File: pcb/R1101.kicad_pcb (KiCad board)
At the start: 2 copper layers, 33 x 51 mm, 4 parts, among them J1 COMPUTE_MOD_1, U1 PHOTON_SMD

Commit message: added silkscreen art
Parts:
- added A1: ART, pluggee:pluggeeLabsIcon-16X8, B.Cu at (150.2, 116.0)
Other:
- board text added: "R1101 v1.0 particle.io Photon Interposer plugg.ee Labs LLC 2017 http://plugg.ee"
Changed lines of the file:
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@@
     (area 125.924999 78.924999 159.075001 130.075001)
     (thickness 1.6)
-    (drawings 11)
+    (drawings 12)
     (tracks 62)
     (zones 0)
-    (modules 4)
+    (modules 5)
     (nets 14)
   )
   (page A4)
   (layers
-    (0 F.Cu signal)
-    (31 B.Cu signal)
+    (0 F.Cu signal hide)
+    (31 B.Cu signal hide)
     (32 B.Adhes user)
     (33 F.Adhes user)
@@
       (net 13 /pUSB-))
   )
+  (module pluggee:pluggeeLabsIcon-16X8 (layer B.Cu)
+    (at 150.2 116 90)
+    (fp_text reference A1 (at 0 0 90) (layer B.SilkS) hide
+      (effects (font (thickness 0.3)) (justify mirror))
+    )
+    (fp_text value ART (at 0.75 0 90) (layer B.SilkS) hide
+      (effects (font (thickness 0.3)) (justify mirror))
+    )
+    (fp_poly (pts (xy 7.9375 2.672447) (xy 7.391846 2.000251) (xy 5.524684 2.00025) (xy 3.657522 2.00025)
+      (xy 3.593078 2.109474) (xy 3.52497 2.195927) (xy 3.432187 2.280637) (xy 3.399991 2.30383)
+      (xy 3.316515 2.352706) (xy 3.240573 2.375634) (xy 3.144042 2.378874) (xy 3.079872 2.375112)
+      (xy 2.891651 2.333311) (xy 2.736834 2.241349) (xy 2.622568 2.10544) (xy 2.556003 1.931796)
+      (xy 2.553114 1.917327) (xy 2.546188 1.737138) (xy 2.590288 1.579105) (xy 2.675815 1.4471)
+      (xy 2.793167 1.344997) (xy 2.932745 1.276667) (xy 3.084946 1.245984) (xy 3.240171 1.25682)
+      (xy 3.38882 1.313047) (xy 3.521291 1.418539) (xy 3.585131 1.501041) (xy 3.661888 1.619251)
+      (xy 5.388818 1.619251) (xy 5.776474 1.618983) (xy 6.104767 1.618114) (xy 6.377835 1.61655)
+      (xy 6.599813 1.614192) (xy 6.774837 1.610945) (xy 6.907042 1.606712) (xy 7.000566 1.601397)
+      (xy 7.059543 1.594903) (xy 7.08811 1.587134) (xy 7.091638 1.579563) (xy 7.065771 1.544591)
+      (xy 7.005869 1.467368) (xy 6.917656 1.355153) (xy 6.806857 1.215207) (xy 6.679194 1.054789)
+      (xy 6.57845 0.928688) (xy 6.089372 0.317501) (xy 4.052748 0.317701) (xy 2.016125 0.317902)
+      (xy 1.962419 0.412289) (xy 1.861679 0.529425) (xy 1.722559 0.611213) (xy 1.562839 0.65194)
+      (xy 1.400298 0.645894) (xy 1.315286 0.620207) (xy 1.142547 0.516676) (xy 1.016597 0.370744)
+      (xy 0.964805 0.264947) (xy 0.929341 0.094751) (xy 0.947704 -0.069007) (xy 1.01162 -0.217747)
+      (xy 1.112814 -0.34289) (xy 1.243011 -0.435856) (xy 1.393938 -0.488067) (xy 1.557318 -0.490942)
+      (xy 1.666226 -0.46231) (xy 1.752506 -0.416273) (xy 1.847441 -0.346197) (xy 1.935782 -0.266066)
+      (xy 2.00228 -0.189862) (xy 2.031684 -0.131569) (xy 2.032 -0.126908) (xy 2.063614 -0.119836)
+      (xy 2.157925 -0.113631) (xy 2.314135 -0.108305) (xy 2.531448 -0.103871) (xy 2.809065 -0.10034)
+      (xy 3.14619 -0.097725) (xy 3.542025 -0.096037) (xy 3.995772 -0.095289) (xy 4.137175 -0.09525)
+      (xy 6.242351 -0.095249) (xy 7.089925 1.003648) (xy 7.9375 2.102545) (xy 7.9375 -0.977376)
+      (xy 7.580312 -1.408741) (xy 7.223125 -1.840105) (xy 5.090399 -1.840802) (xy 2.957674 -1.8415)
+      (xy 2.922728 -1.735612) (xy 2.845738 -1.592506) (xy 2.729856 -1.488125) (xy 2.587116 -1.423263)
+      (xy 2.429552 -1.398715) (xy 2.269197 -1.415274) (xy 2.118086 -1.473735) (xy 1.988253 -1.574891)
+      (xy 1.91778 -1.669291) (xy 1.850254 -1.839804) (xy 1.839916 -2.010188) (xy 1.881276 -2.170131)
+      (xy 1.968845 -2.309316) (xy 2.097132 -2.417429) (xy 2.260649 -2.484157) (xy 2.359484 -2.499199)
+      (xy 2.540921 -2.482357) (xy 2.701006 -2.407286) (xy 2.832592 -2.277645) (xy 2.854881 -2.245459)
+      (xy 2.931638 -2.12725) (xy 5.162894 -2.12725) (xy 5.59363 -2.127189) (xy 5.965311 -2.126931)
+      (xy 6.282381 -2.126361) (xy 6.549286 -2.125366) (xy 6.770468 -2.123831) (xy 6.950374 -2.121642)
+      (xy 7.093448 -2.118685) (xy 7.204134 -2.114845) (xy 7.286877 -2.110009) (xy 7.346122 -2.104062)
+      (xy 7.386313 -2.096891) (xy 7.411895 -2.08838) (xy 7.427313 -2.078416) (xy 7.435637 -2.068873)
+      (xy 7.47392 -2.021825) (xy 7.544397 -1.941065) (xy 7.635882 -1.839258) (xy 7.707312 -1.761298)
+      (xy 7.9375 -1.512098) (xy 7.9375 -4.15925) (xy -7.9375 -4.15925) (xy -7.9375 -2.688196)
+      (xy -7.509706 -2.12725) (xy -5.63124 -2.12725) (xy -3.752773 -2.127249) (xy -3.688329 -2.236473)
+      (xy -3.571643 -2.37785) (xy -3.423244 -2.472213) (xy -3.255893 -2.515964) (xy -3.082352 -2.505506)
+      (xy -2.935025 -2.448817) (xy -2.78592 -2.335518) (xy -2.692871 -2.193123) (xy -2.653784 -2.018042)
+      (xy -2.652212 -1.964385) (xy -2.658491 -1.84716) (xy -2.681995 -1.763529) (xy -2.73228 -1.684047)
+      (xy -2.750828 -1.660542) (xy -2.881344 -1.528115) (xy -3.019707 -1.451293) (xy -3.180728 -1.422562)
+      (xy -3.221213 -1.421954) (xy -3.40284 -1.448299) (xy -3.555673 -1.51942) (xy -3.669787 -1.628645)
+      (xy -3.734757 -1.767283) (xy -3.753384 -1.8415) (xy -5.480317 -1.8415) (xy -5.804828 -1.84115)
+      (xy -6.109463 -1.840144) (xy -6.38846 -1.838547) (xy -6.636056 -1.836426) (xy -6.846485 -1.833845)
+      (xy -7.013986 -1.830869) (xy -7.132794 -1.827565) (xy -7.197146 -1.823999) (xy -7.207251 -1.821876)
+      (xy -7.189178 -1.792127) (xy -7.138199 -1.718128) (xy -7.059177 -1.606677) (xy -6.956972 -1.464575)
+      (xy -6.836444 -1.298619) (xy -6.702454 -1.115609) (xy -6.696495 -1.107501) (xy -6.185739 -0.41275)
+      (xy -2.125889 -0.41275) (xy -2.090247 -0.490975) (xy -2.027738 -0.573654) (xy -1.924235 -0.657612)
+      (xy -1.800249 -0.728336) (xy -1.703337 -0.76475) (xy -1.545731 -0.777984) (xy -1.393042 -0.737467)
+      (xy -1.255042 -0.652763) (xy -1.141503 -0.533435) (xy -1.062197 -0.389048) (xy -1.026896 -0.229165)
+      (xy -1.034201 -0.109895) (xy -1.094207 0.056773) (xy -1.199417 0.19582) (xy -1.337729 0.299435)
+      (xy -1.497039 0.359809) (xy -1.665245 0.36913) (xy -1.74984 0.351926) (xy -1.85936 0.303082)
+      (xy -1.968986 0.228669) (xy -2.059232 0.144309) (xy -2.110612 0.065628) (xy -2.111996 0.061545)
+      (xy -2.117415 0.049345) (xy -2.12838 0.038873) (xy -2.149438 0.029997) (xy -2.185134 0.022586)
+      (xy -2.240013 0.016507) (xy -2.318623 0.01163) (xy -2.425507 0.00782) (xy -2.565212 0.004948)
+      (xy -2.742284 0.002881) (xy -2.961268 0.001487) (xy -3.226711 0.000633) (xy -3.543157 0.000189)
+      (xy -3.915152 0.000023) (xy -4.232906 0) (xy -6.334282 0) (xy -7.096204 -1.005741)
+      (xy -7.264754 -1.228202) (xy -7.422305 -1.436092) (xy -7.564506 -1.623676) (xy -7.687006 -1.785216)
+      (xy -7.785453 -1.914975) (xy -7.855499 -2.007217) (xy -7.892791 -2.056203) (xy -7.896803 -2.061429)
+      (xy -7.907366 -2.063054) (xy -7.91597 -2.034729) (xy -7.922793 -1.971604) (xy -7.928017 -1.868832)
+      (xy -7.931821 -1.72156) (xy -7.934385 -1.524941) (xy -7.935889 -1.274125) (xy -7.936491 -0.992187)
+      (xy -7.9375 0.127) (xy -7.33864 0.127) (xy -6.661758 0.919663) (xy -5.984875 1.712326)
+      (xy -3.836949 1.713413) (xy -1.689023 1.714501) (xy -1.624579 1.605277) (xy -1.511671 1.469556)
+      (xy -1.363986 1.373267) (xy -1.198946 1.326564) (xy -1.141587 1.323789) (xy -0.969591 1.351361)
+      (xy -0.819933 1.431996) (xy -0.689389 1.562438) (xy -0.604399 1.712563) (xy -0.574047 1.873662)
+      (xy -0.593346 2.034858) (xy -0.657311 2.185273) (xy -0.760959 2.314027) (xy -0.899304 2.410244)
+      (xy -1.067361 2.463044) (xy -1.104094 2.467437) (xy -1.265806 2.454635) (xy -1.421591 2.395068)
+      (xy -1.550438 2.298656) (xy -1.603375 2.231661) (xy -1.666875 2.129697) (xy -3.893755 2.128474)
+      (xy -6.120634 2.12725) (xy -6.811924 1.317625) (xy -7.503215 0.508) (xy -7.9375 0.508)
+      (xy -7.9375 4.15925) (xy 7.9375 4.15925) (xy 7.9375 2.672447)) (layer B.SilkS) (width 0.01))
+  )
+  (gr_text "R1101 v1.0\nparticle.io Photon Interposer\nplugg.ee Labs LLC 2017\nhttp://plugg.ee" (at 141.2 124.2 270) (layer B.SilkS)
+    (effects (font (size 1.2 1.2) (thickness 0.2)) (justify left mirror))
+  )
   (gr_arc (start 128 128) (end 128 130) (angle 90) (layer Edge.Cuts) (width 0.15))

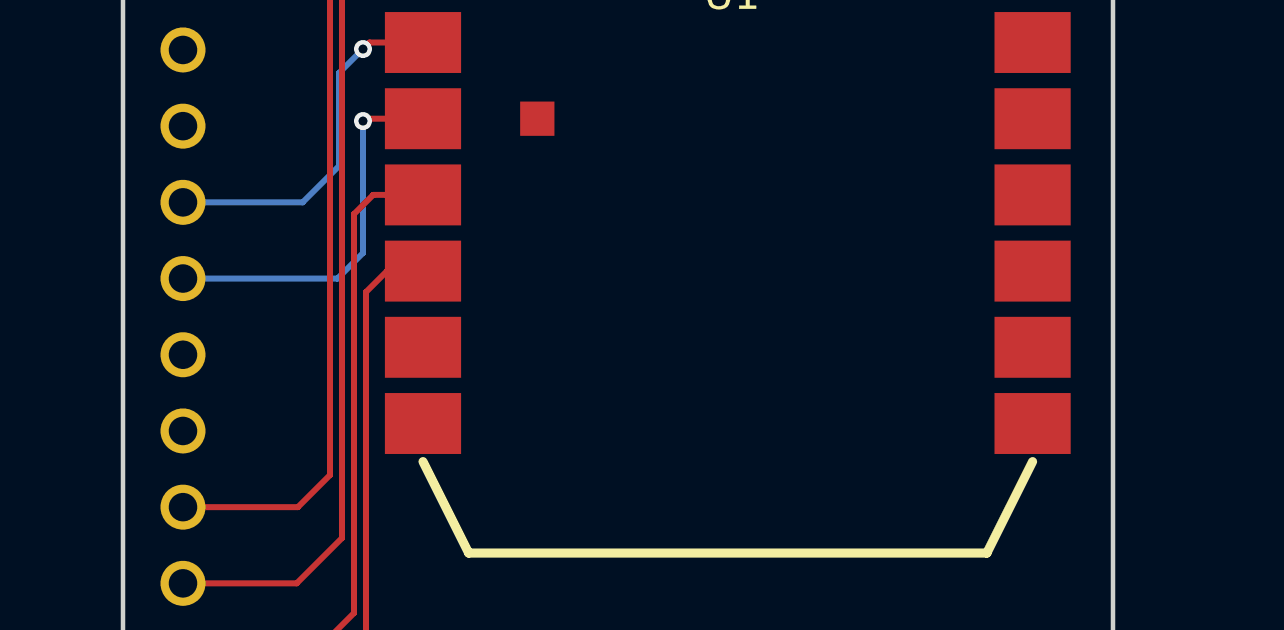
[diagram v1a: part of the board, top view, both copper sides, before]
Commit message: connected I2C
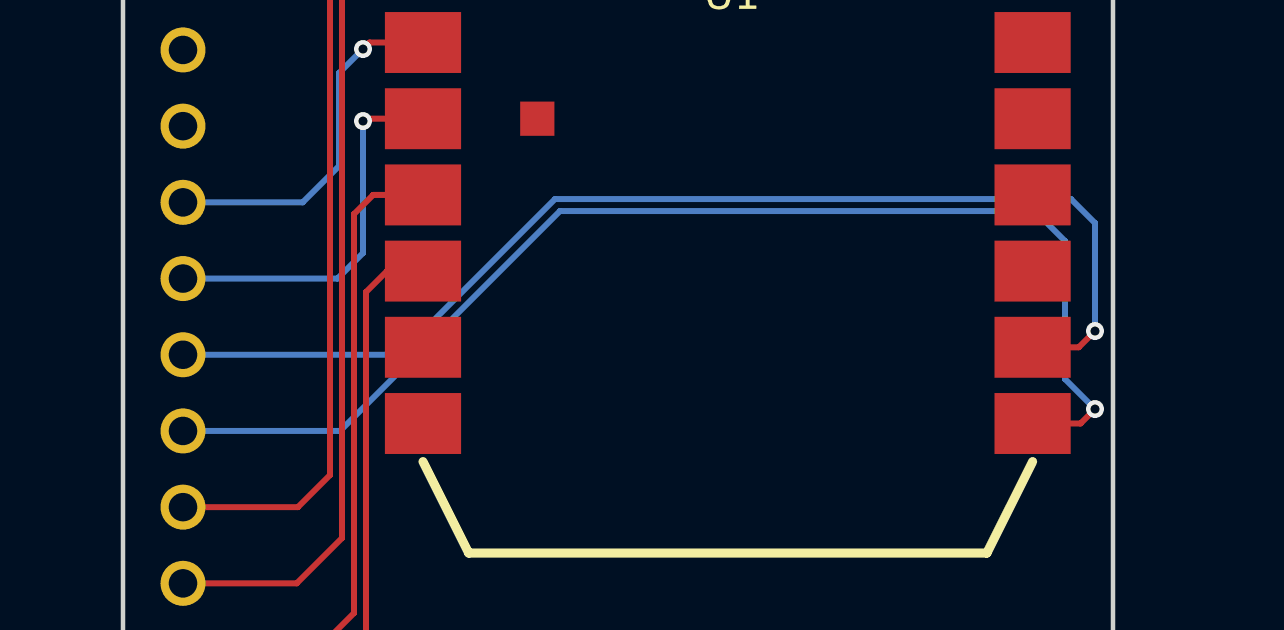
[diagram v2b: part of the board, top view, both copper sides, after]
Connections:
- J1 pad 11: (no net) -> /SCK
- J1 pad 12: (no net) -> /SDA
- U1 pad 13: (no net) -> /SDA
- U1 pad 14: (no net) -> /SCK
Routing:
- net /SDA: track 0.00 -> 41.1 mm, vias 0 -> 1
- net /SCK: track 0.00 -> 38.8 mm, vias 0 -> 1
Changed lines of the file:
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@@
 (kicad_pcb (version 4) (host pcbnew 4.0.6-e0-6349~53~ubuntu14.04.1)
   (general
-    (links 15)
+    (links 17)
     (no_connects 0)
     (area 125.924999 78.924999 159.075001 130.075001)
     (thickness 1.6)
     (drawings 12)
-    (tracks 62)
+    (tracks 79)
     (zones 0)
     (modules 5)
-    (nets 14)
+    (nets 16)
   )
   (page A4)
   (layers
-    (0 F.Cu signal hide)
-    (31 B.Cu signal hide)
+    (0 F.Cu signal)
+    (31 B.Cu signal)
     (32 B.Adhes user)
     (33 F.Adhes user)
@@
   (net 12 /pUSB+)
   (net 13 /pUSB-)
+  (net 14 /SCK)
+  (net 15 /SDA)
   (net_class Default "This is the default net class."
     (clearance 0.2)
@@
     (add_net /P0[25])
     (add_net /P0[26])
+    (add_net /SCK)
+    (add_net /SDA)
     (add_net /SYSRXD0-PHOTONTX)
     (add_net /SYSTXD0-PHOTONRX)
@@
     (pad 10 thru_hole circle (at 0 6.35) (size 1.5 1.5) (drill 0.95) (layers *.Cu *.Mask)
       (net 7 /~ISP))
-    (pad 11 thru_hole circle (at 0 8.89) (size 1.5 1.5) (drill 0.95) (layers *.Cu *.Mask))
-    (pad 12 thru_hole circle (at 0 11.43) (size 1.5 1.5) (drill 0.95) (layers *.Cu *.Mask))
+    (pad 11 thru_hole circle (at 0 8.89) (size 1.5 1.5) (drill 0.95) (layers *.Cu *.Mask)
+      (net 14 /SCK))
+    (pad 12 thru_hole circle (at 0 11.43) (size 1.5 1.5) (drill 0.95) (layers *.Cu *.Mask)
+      (net 15 /SDA))
     (pad 13 thru_hole circle (at 0 13.97) (size 1.5 1.5) (drill 0.95) (layers *.Cu *.Mask)
       (net 8 /SYSRXD0-PHOTONTX))
@@
     (pad 11 smd rect (at 0 -6.858) (size 2.54 2.032) (layers F.Cu F.Paste F.Mask))
     (pad 12 smd rect (at 0 -4.318) (size 2.54 2.032) (layers F.Cu F.Paste F.Mask))
-    (pad 13 smd rect (at 20.32 -4.318) (size 2.54 2.032) (layers F.Cu F.Paste F.Mask))
-    (pad 14 smd rect (at 20.32 -6.858) (size 2.54 2.032) (layers F.Cu F.Paste F.Mask))
+    (pad 13 smd rect (at 20.32 -4.318) (size 2.54 2.032) (layers F.Cu F.Paste F.Mask)
+      (net 15 /SDA))
+    (pad 14 smd rect (at 20.32 -6.858) (size 2.54 2.032) (layers F.Cu F.Paste F.Mask)
+      (net 14 /SCK))
     (pad 15 smd rect (at 20.32 -9.398) (size 2.54 2.032) (layers F.Cu F.Paste F.Mask))
     (pad 16 smd rect (at 20.32 -11.938) (size 2.54 2.032) (layers F.Cu F.Paste F.Mask))
@@
   (segment (start 146.8 84.3) (end 143.7 84.3) (width 0.2) (layer F.Cu) (net 13))
   (segment (start 147.176 83.924) (end 146.8 84.3) (width 0.2) (layer F.Cu) (net 13))
+  (segment (start 156.32 111.142) (end 157.858 111.142) (width 0.2) (layer F.Cu) (net 14))
+  (segment (start 135.21 111.39) (end 128 111.39) (width 0.2) (layer B.Cu) (net 14))
+  (segment (start 140.4 106.2) (end 135.21 111.39) (width 0.2) (layer B.Cu) (net 14))
+  (segment (start 157.6 106.2) (end 140.4 106.2) (width 0.2) (layer B.Cu) (net 14))
+  (segment (start 158.4 107) (end 157.6 106.2) (width 0.2) (layer B.Cu) (net 14))
+  (segment (start 158.4 110.6) (end 158.4 107) (width 0.2) (layer B.Cu) (net 14))
+  (via (at 158.4 110.6) (size 0.6) (drill 0.3) (layers F.Cu B.Cu) (net 14))
+  (segment (start 157.858 111.142) (end 158.4 110.6) (width 0.2) (layer F.Cu) (net 14))
+  (segment (start 156.32 113.682) (end 157.918 113.682) (width 0.2) (layer F.Cu) (net 15))
+  (segment (start 133.235688 113.93) (end 128 113.93) (width 0.2) (layer B.Cu) (net 15))
+  (segment (start 140.565686 106.600002) (end 133.235688 113.93) (width 0.2) (layer B.Cu) (net 15))
+  (segment (start 156.400002 106.600002) (end 140.565686 106.600002) (width 0.2) (layer B.Cu) (net 15))
+  (segment (start 157.4 107.6) (end 156.400002 106.600002) (width 0.2) (layer B.Cu) (net 15))
+  (segment (start 157.4 112.2) (end 157.4 107.6) (width 0.2) (layer B.Cu) (net 15))
+  (segment (start 158.4 113.2) (end 157.4 112.2) (width 0.2) (layer B.Cu) (net 15))
+  (via (at 158.4 113.2) (size 0.6) (drill 0.3) (layers F.Cu B.Cu) (net 15))
+  (segment (start 157.918 113.682) (end 158.4 113.2) (width 0.2) (layer F.Cu) (net 15))
   (zone (net 1) (net_name GND) (layer B.Cu) (hatch edge 0.508)
     (connect_pads (clearance 0.22))

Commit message: updated SWD signal naming
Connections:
- net /P0[25] renamed /SWDIO
- net /P0[26] renamed /SWDCLK
